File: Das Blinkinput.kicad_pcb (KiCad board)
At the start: 2 copper layers, 50.8 x 12.7 mm, 37 parts, among them P101 CONN_01X02, P102 CONN_01X01, P103 CONN_01X01, P104 CONN_01X01, P105 CONN_01X05, P201 CONN_01X01, P301 CONN_01X01, P401 CONN_01X01, P501 CONN_01X01, U101 LP2980IM5-3.0/NOPB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

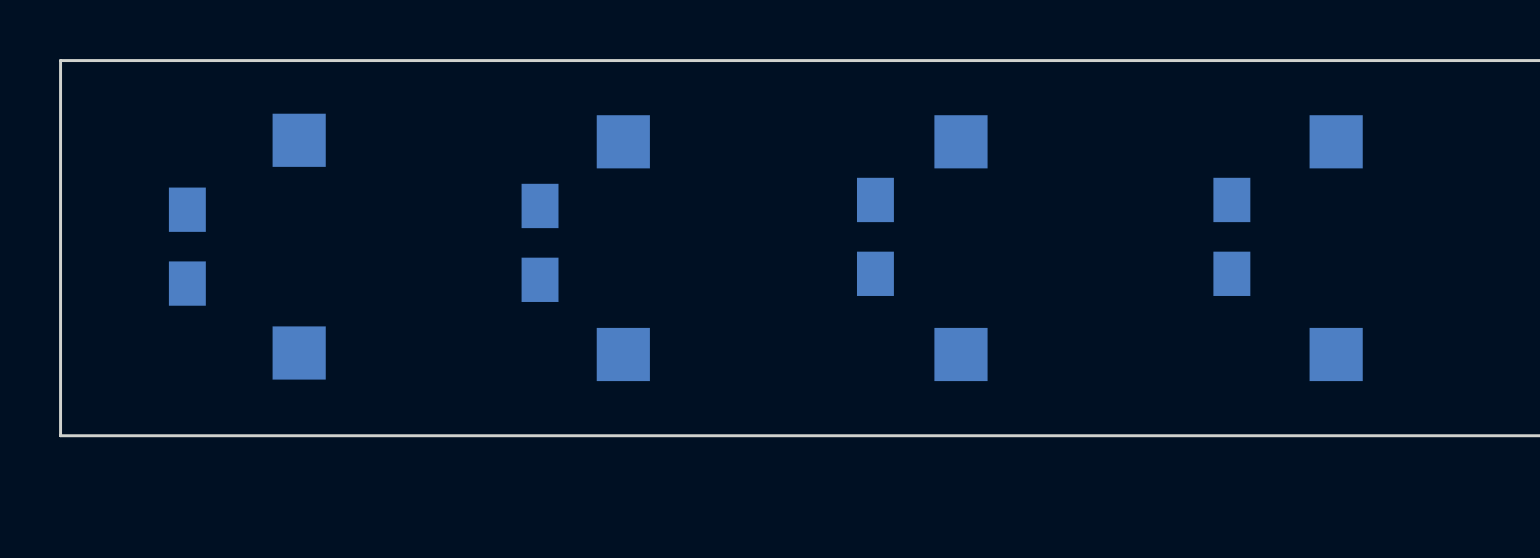
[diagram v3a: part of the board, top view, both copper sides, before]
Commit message: Removing extra set of photodiodes and changing the original photodiode footprint
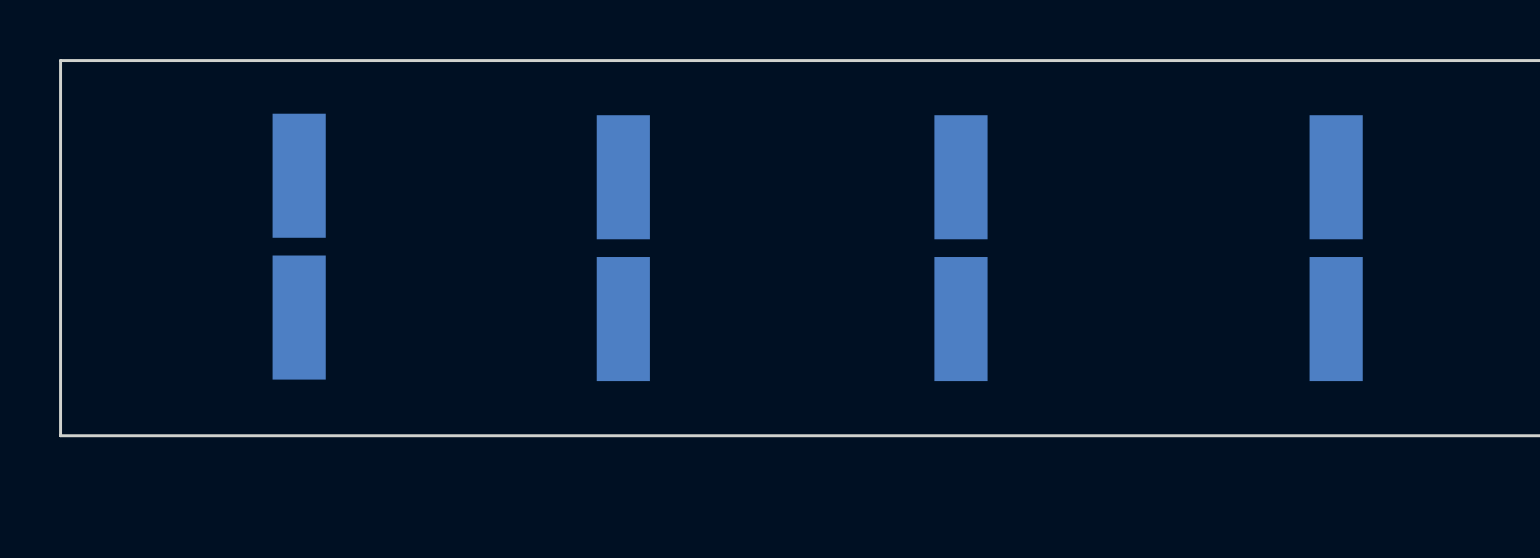
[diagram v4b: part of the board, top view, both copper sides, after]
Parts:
- removed PD202, PD302, PD402, PD502: NOPOP, Capacitors_SMD:C_0805_HandSoldering
- PD201, PD301, PD401, PD501: footprint DasBlinkinput:VPW34SR -> DasBlinkinput:VPW34SR*
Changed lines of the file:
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@@
 (kicad_pcb (version 4) (host pcbnew 0.201505141916+5653~23~ubuntu14.04.1-product)
   (general
-    (links 77)
-    (no_connects 77)
+    (links 69)
+    (no_connects 69)
     (area 77.419999 105.359999 128.320001 118.160001)
     (thickness 1.6)
@@
     (tracks 0)
     (zones 0)
-    (modules 37)
+    (modules 33)
     (nets 21)
   )
@@
     )
   )
-  (module DasBlinkinput:VPW34SR (layer B.Cu)
+  (module DasBlinkinput:VPW34SR* (layer B.Cu)
     (at 85.5472 111.7092 90)
     (fp_text reference PD201 (at 0 -3.5 90) (layer B.SilkS)
       (effects (font (size 1 1) (thickness 0.15)) (justify mirror))
     )
-    (fp_text value VBPW34SR (at -0.1 4.8 90) (layer B.Fab)
+    (fp_text value VBPW34SR (at 0.3 3.3 90) (layer B.Fab)
       (effects (font (size 1 1) (thickness 0.15)) (justify mirror))
     )
@@
     (fp_line (start 2 2.2) (end 2 -2.2) (layer B.SilkS) (width 0.15))
     (fp_line (start -2 2.2) (end 2 2.2) (layer B.SilkS) (width 0.15))
-    (pad 1 smd rect (at -3.6 0 90) (size 1.8 1.8) (layers B.Cu B.Paste B.Mask)
+    (pad 1 smd rect (at -2.4 0 90) (size 4.2 1.8) (layers B.Cu B.Paste B.Mask)
       (net 12 VGND))
-    (pad 2 smd rect (at 3.6 0 90) (size 1.8 1.8) (layers B.Cu B.Paste B.Mask)
+    (pad 2 smd rect (at 2.4 0 90) (size 4.2 1.8) (layers B.Cu B.Paste B.Mask)
       (net 5 "Net-(C202-Pad2)"))
   )
-  (module DasBlinkinput:VPW34SR (layer B.Cu)
+  (module DasBlinkinput:VPW34SR* (layer B.Cu)
     (at 107.95 111.76 90)
     (fp_text reference PD301 (at 0 -3.5 90) (layer B.SilkS)
       (effects (font (size 1 1) (thickness 0.15)) (justify mirror))
     )
-    (fp_text value VBPW34SR (at -0.1 4.8 90) (layer B.Fab)
+    (fp_text value VBPW34SR (at 0.3 3.3 90) (layer B.Fab)
       (effects (font (size 1 1) (thickness 0.15)) (justify mirror))
     )
@@
     (fp_line (start 2 2.2) (end 2 -2.2) (layer B.SilkS) (width 0.15))
     (fp_line (start -2 2.2) (end 2 2.2) (layer B.SilkS) (width 0.15))
-    (pad 1 smd rect (at -3.6 0 90) (size 1.8 1.8) (layers B.Cu B.Paste B.Mask)
+    (pad 1 smd rect (at -2.4 0 90) (size 4.2 1.8) (layers B.Cu B.Paste B.Mask)
       (net 12 VGND))
-    (pad 2 smd rect (at 3.6 0 90) (size 1.8 1.8) (layers B.Cu B.Paste B.Mask)
+    (pad 2 smd rect (at 2.4 0 90) (size 4.2 1.8) (layers B.Cu B.Paste B.Mask)
       (net 7 "Net-(C301-Pad2)"))
   )
-  (module DasBlinkinput:VPW34SR (layer B.Cu)
+  (module DasBlinkinput:VPW34SR* (layer B.Cu)
     (at 120.65 111.76 90)
     (fp_text reference PD401 (at 0 -3.5 90) (layer B.SilkS)
       (effects (font (size 1 1) (thickness 0.15)) (justify mirror))
     )
-    (fp_text value VBPW34SR (at -0.1 4.8 90) (layer B.Fab)
+    (fp_text value VBPW34SR (at 0.3 3.3 90) (layer B.Fab)
       (effects (font (size 1 1) (thickness 0.15)) (justify mirror))
     )
@@
     (fp_line (start 2 2.2) (end 2 -2.2) (layer B.SilkS) (width 0.15))
     (fp_line (start -2 2.2) (end 2 2.2) (layer B.SilkS) (width 0.15))
-    (pad 1 smd rect (at -3.6 0 90) (size 1.8 1.8) (layers B.Cu B.Paste B.Mask)
+    (pad 1 smd rect (at -2.4 0 90) (size 4.2 1.8) (layers B.Cu B.Paste B.Mask)
       (net 12 VGND))
-    (pad 2 smd rect (at 3.6 0 90) (size 1.8 1.8) (layers B.Cu B.Paste B.Mask)
+    (pad 2 smd rect (at 2.4 0 90) (size 4.2 1.8) (layers B.Cu B.Paste B.Mask)
       (net 9 "Net-(C401-Pad2)"))
   )
-  (module DasBlinkinput:VPW34SR (layer B.Cu)
+  (module DasBlinkinput:VPW34SR* (layer B.Cu)
     (at 96.52 111.76 90)
     (fp_text reference PD501 (at 0 -3.5 90) (layer B.SilkS)
       (effects (font (size 1 1) (thickness 0.15)) (justify mirror))
     )
-    (fp_text value VBPW34SR (at -0.1 4.8 90) (layer B.Fab)
+    (fp_text value VBPW34SR (at 0.3 3.3 90) (layer B.Fab)
       (effects (font (size 1 1) (thickness 0.15)) (justify mirror))
     )
@@
     (fp_line (start 2 2.2) (end 2 -2.2) (layer B.SilkS) (width 0.15))
     (fp_line (start -2 2.2) (end 2 2.2) (layer B.SilkS) (width 0.15))
-    (pad 1 smd rect (at -3.6 0 90) (size 1.8 1.8) (layers B.Cu B.Paste B.Mask)
+    (pad 1 smd rect (at -2.4 0 90) (size 4.2 1.8) (layers B.Cu B.Paste B.Mask)
       (net 12 VGND))
-    (pad 2 smd rect (at 3.6 0 90) (size 1.8 1.8) (layers B.Cu B.Paste B.Mask)
+    (pad 2 smd rect (at 2.4 0 90) (size 4.2 1.8) (layers B.Cu B.Paste B.Mask)
       (net 11 "Net-(C501-Pad2)"))
   )
-  (module Capacitors_SMD:C_0805_HandSoldering (layer B.Cu)
-    (at 81.7626 111.7092 90)
-    (descr "Capacitor SMD 0805, hand soldering")
-    (tags "capacitor 0805")
-    (attr smd)
-    (fp_text reference PD202 (at 0 2.1 90) (layer B.SilkS)
-      (effects (font (size 1 1) (thickness 0.15)) (justify mirror))
-    )
-    (fp_text value NOPOP (at 0 -2.1 90) (layer B.Fab)
-      (effects (font (size 1 1) (thickness 0.15)) (justify mirror))
-    )
-    (fp_line (start -2.3 1) (end 2.3 1) (layer B.CrtYd) (width 0.05))
-    (fp_line (start -2.3 -1) (end 2.3 -1) (layer B.CrtYd) (width 0.05))
-    (fp_line (start -2.3 1) (end -2.3 -1) (layer B.CrtYd) (width 0.05))
-    (fp_line (start 2.3 1) (end 2.3 -1) (layer B.CrtYd) (width 0.05))
-    (fp_line (start 0.5 0.85) (end -0.5 0.85) (layer B.SilkS) (width 0.15))
-    (fp_line (start -0.5 -0.85) (end 0.5 -0.85) (layer B.SilkS) (width 0.15))
-    (pad 1 smd rect (at -1.25 0 90) (size 1.5 1.25) (layers B.Cu B.Paste B.Mask)
-      (net 12 VGND))
-    (pad 2 smd rect (at 1.25 0 90) (size 1.5 1.25) (layers B.Cu B.Paste B.Mask)
-      (net 5 "Net-(C202-Pad2)"))
-    (model Capacitors_SMD.3dshapes/C_0805_HandSoldering.wrl
-      (at (xyz 0 0 0))
-      (scale (xyz 1 1 1))
-      (rotate (xyz 0 0 0))
-    )
-  )
-  (module Capacitors_SMD:C_0805_HandSoldering (layer B.Cu)
-    (at 105.0544 111.379 90)
-    (descr "Capacitor SMD 0805, hand soldering")
-    (tags "capacitor 0805")
-    (attr smd)
-    (fp_text reference PD302 (at 0 2.1 90) (layer B.SilkS)
-      (effects (font (size 1 1) (thickness 0.15)) (justify mirror))
-    )
-    (fp_text value NOPOP (at 0 -2.1 90) (layer B.Fab)
-      (effects (font (size 1 1) (thickness 0.15)) (justify mirror))
-    )
-    (fp_line (start -2.3 1) (end 2.3 1) (layer B.CrtYd) (width 0.05))
-    (fp_line (start -2.3 -1) (end 2.3 -1) (layer B.CrtYd) (width 0.05))
-    (fp_line (start -2.3 1) (end -2.3 -1) (layer B.CrtYd) (width 0.05))
-    (fp_line (start 2.3 1) (end 2.3 -1) (layer B.CrtYd) (width 0.05))
-    (fp_line (start 0.5 0.85) (end -0.5 0.85) (layer B.SilkS) (width 0.15))
-    (fp_line (start -0.5 -0.85) (end 0.5 -0.85) (layer B.SilkS) (width 0.15))
-    (pad 1 smd rect (at -1.25 0 90) (size 1.5 1.25) (layers B.Cu B.Paste B.Mask)
-      (net 12 VGND))
-    (pad 2 smd rect (at 1.25 0 90) (size 1.5 1.25) (layers B.Cu B.Paste B.Mask)
-      (net 7 "Net-(C301-Pad2)"))
-    (model Capacitors_SMD.3dshapes/C_0805_HandSoldering.wrl
-      (at (xyz 0 0 0))
-      (scale (xyz 1 1 1))
-      (rotate (xyz 0 0 0))
-    )
-  )
-  (module Capacitors_SMD:C_0805_HandSoldering (layer B.Cu)
-    (at 117.1194 111.379 90)
-    (descr "Capacitor SMD 0805, hand soldering")
-    (tags "capacitor 0805")
-    (attr smd)
-    (fp_text reference PD402 (at 0 2.1 90) (layer B.SilkS)
-      (effects (font (size 1 1) (thickness 0.15)) (justify mirror))
-    )
-    (fp_text value NOPOP (at 0 -2.1 90) (layer B.Fab)
-      (effects (font (size 1 1) (thickness 0.15)) (justify mirror))
-    )
-    (fp_line (start -2.3 1) (end 2.3 1) (layer B.CrtYd) (width 0.05))
-    (fp_line (start -2.3 -1) (end 2.3 -1) (layer B.CrtYd) (width 0.05))
-    (fp_line (start -2.3 1) (end -2.3 -1) (layer B.CrtYd) (width 0.05))
-    (fp_line (start 2.3 1) (end 2.3 -1) (layer B.CrtYd) (width 0.05))
-    (fp_line (start 0.5 0.85) (end -0.5 0.85) (layer B.SilkS) (width 0.15))
-    (fp_line (start -0.5 -0.85) (end 0.5 -0.85) (layer B.SilkS) (width 0.15))
-    (pad 1 smd rect (at -1.25 0 90) (size 1.5 1.25) (layers B.Cu B.Paste B.Mask)
-      (net 12 VGND))
-    (pad 2 smd rect (at 1.25 0 90) (size 1.5 1.25) (layers B.Cu B.Paste B.Mask)
-      (net 9 "Net-(C401-Pad2)"))
-    (model Capacitors_SMD.3dshapes/C_0805_HandSoldering.wrl
-      (at (xyz 0 0 0))
-      (scale (xyz 1 1 1))
-      (rotate (xyz 0 0 0))
-    )
-  )
-  (module Capacitors_SMD:C_0805_HandSoldering (layer B.Cu)
-    (at 93.7006 111.5822 90)
-    (descr "Capacitor SMD 0805, hand soldering")
-    (tags "capacitor 0805")
-    (attr smd)
-    (fp_text reference PD502 (at 0 2.1 90) (layer B.SilkS)
-      (effects (font (size 1 1) (thickness 0.15)) (justify mirror))
-    )
-    (fp_text value NOPOP (at 0 -2.1 90) (layer B.Fab)
-      (effects (font (size 1 1) (thickness 0.15)) (justify mirror))
-    )
-    (fp_line (start -2.3 1) (end 2.3 1) (layer B.CrtYd) (width 0.05))
-    (fp_line (start -2.3 -1) (end 2.3 -1) (layer B.CrtYd) (width 0.05))
-    (fp_line (start -2.3 1) (end -2.3 -1) (layer B.CrtYd) (width 0.05))
-    (fp_line (start 2.3 1) (end 2.3 -1) (layer B.CrtYd) (width 0.05))
-    (fp_line (start 0.5 0.85) (end -0.5 0.85) (layer B.SilkS) (width 0.15))
-    (fp_line (start -0.5 -0.85) (end 0.5 -0.85) (layer B.SilkS) (width 0.15))
-    (pad 1 smd rect (at -1.25 0 90) (size 1.5 1.25) (layers B.Cu B.Paste B.Mask)
-      (net 12 VGND))
-    (pad 2 smd rect (at 1.25 0 90) (size 1.5 1.25) (layers B.Cu B.Paste B.Mask)
-      (net 11 "Net-(C501-Pad2)"))
-    (model Capacitors_SMD.3dshapes/C_0805_HandSoldering.wrl
-      (at (xyz 0 0 0))
-      (scale (xyz 1 1 1))
-      (rotate (xyz 0 0 0))
-    )
-  )
   (gr_line (start 77.47 105.41) (end 77.47 118.11) (angle 90) (layer Edge.Cuts) (width 0.1))

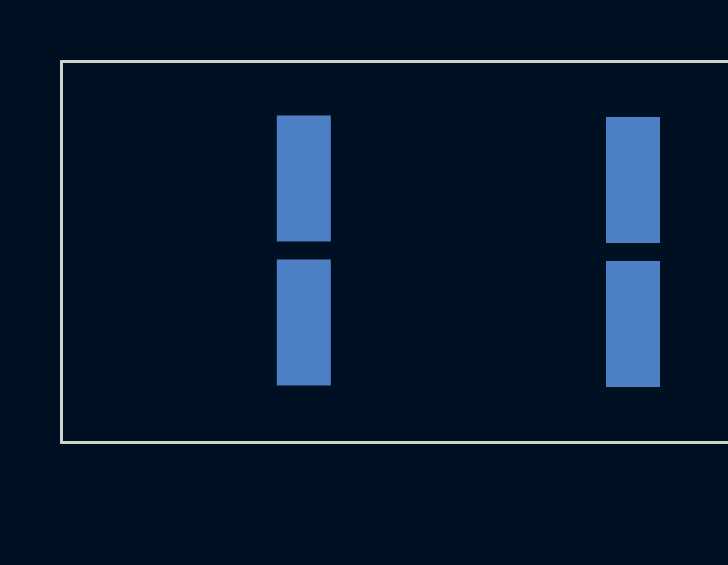
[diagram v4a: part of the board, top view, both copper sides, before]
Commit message: Schematic and layout cleanup after photodiode removal
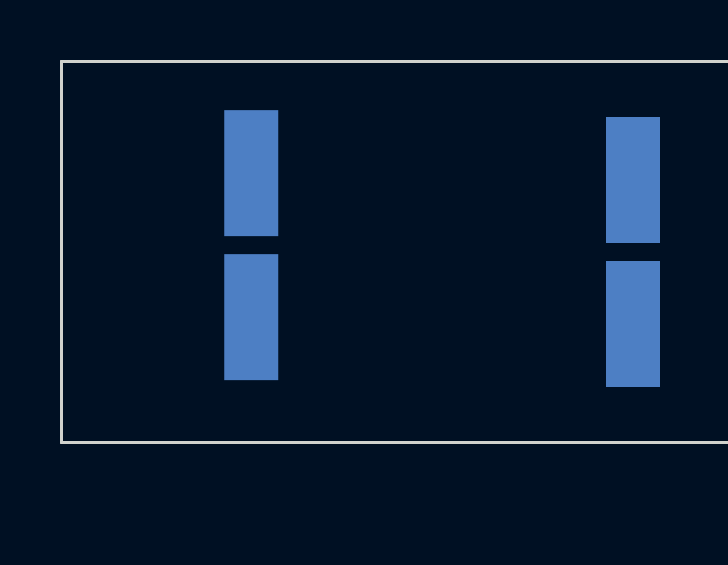
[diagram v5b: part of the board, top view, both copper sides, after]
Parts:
- moved PD201 1.76 mm to (83.8, 111.5)
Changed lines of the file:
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@@
   )
   (module DasBlinkinput:VPW34SR* (layer B.Cu)
-    (at 85.5472 111.7092 90)
+    (at 83.7946 111.5314 90)
     (fp_text reference PD201 (at 0 -3.5 90) (layer B.SilkS)
       (effects (font (size 1 1) (thickness 0.15)) (justify mirror))

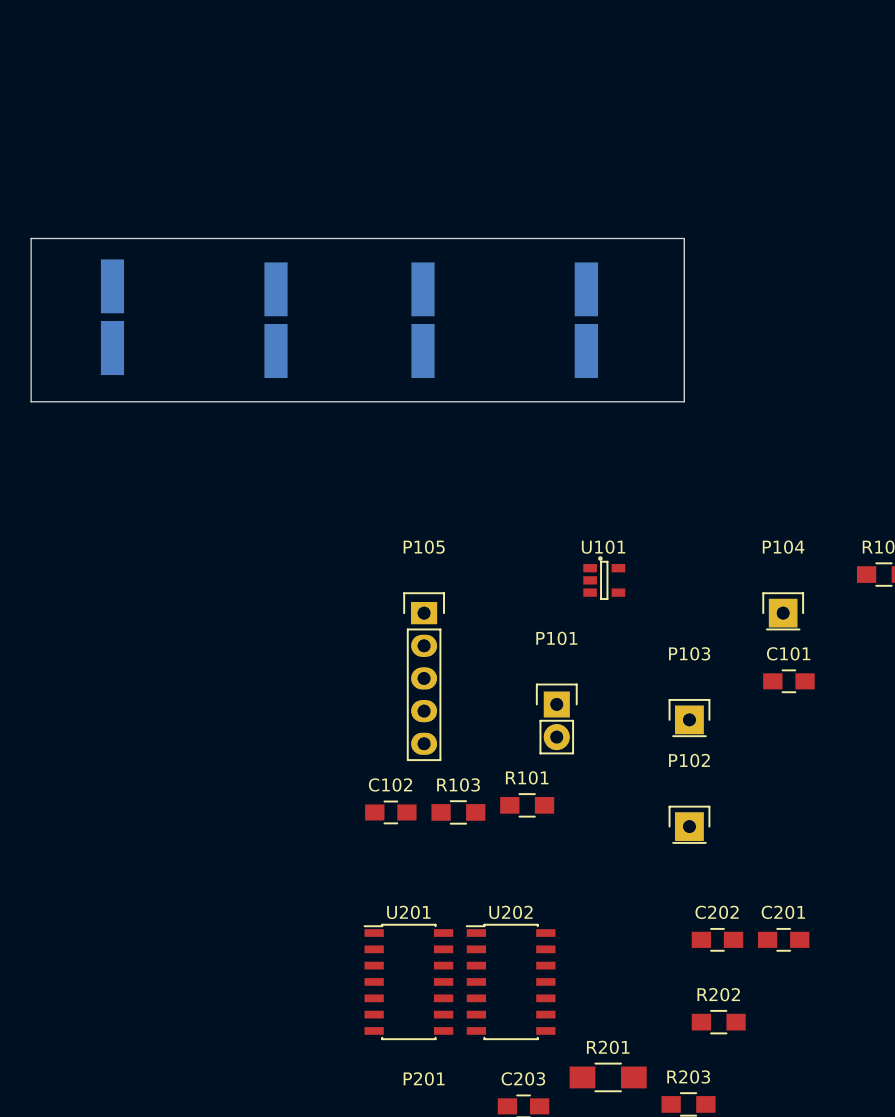
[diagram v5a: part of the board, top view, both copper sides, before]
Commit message: Increased board size to 2 sq inches and layer count to 4
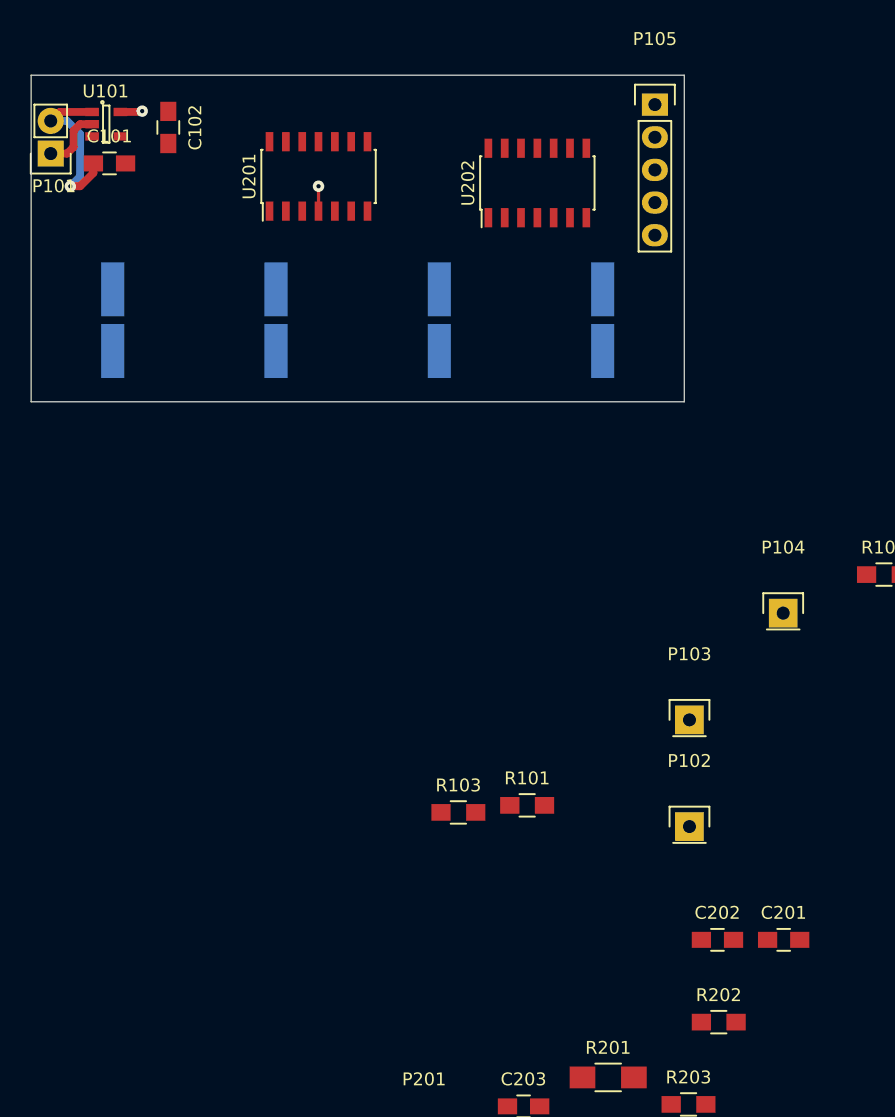
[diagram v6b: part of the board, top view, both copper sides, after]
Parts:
- moved C101 66.4 mm to (83.6, 99.6)
- moved U201 63.0 mm to (99.8, 100.6), turned to 90 degrees
- moved U202 62.2 mm to (116.8, 101.1), turned to 90 degrees
- moved P101 58.2 mm to (79.0, 98.8), turned to 180 degrees
- moved C102 56.0 mm to (88.1, 96.8), turned to 270 degrees
- moved U101 52.5 mm to (83.3, 96.5)
- moved P105 43.4 mm to (126.0, 95.0)
- moved PD301 1.27 mm to (109.2, 111.8)
- moved PD401 1.27 mm to (121.9, 111.8)
- moved PD201 0.23 mm to (83.8, 111.8)
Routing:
- net Net-(C101-Pad1): track 0.00 -> 13.6 mm, vias 0 -> 1
- net GND: track 0.00 -> 4.91 mm
- net 3V: track 0.00 -> 3.66 mm, vias 0 -> 2
- added copper zone on PWR.Cu, net 3V
- added copper zone on GND.Cu, net GND
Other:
- board size 50.8 x 12.7 mm -> 50.8 x 25.4 mm
- copper layers 2 -> 4
- net class Default: clearance 0.254 -> 0.1524; trace_width 0.254 -> 0.1524; via_dia 0.889 -> 0.6858; via_drill 0.635 -> 0.3302
- net class Power added: clearance 0.254, trace_width 0.6096, via_dia 0.889, via_drill 0.4572
- rule trace_clearance: 0.254 -> 0.1524
- rule trace_min: 0.254 -> 0.1524
- rule via_min_drill: 0.508 -> 0.3302
- rule via_min_size: 0.889 -> 0.6858
